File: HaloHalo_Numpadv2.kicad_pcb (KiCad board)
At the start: 2 copper layers, 108.7 x 105.4 mm, 92 parts, among them SW1 SW_SPST, SW10 SW_SPST, SW11 SW_SPST, SW12 SW_SPST, SW13 SW_SPST, SW14 SW_SPST, SW15 SW_SPST, SW16 SW_SPST, SW17 SW_SPST, SW18 SW_SPST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

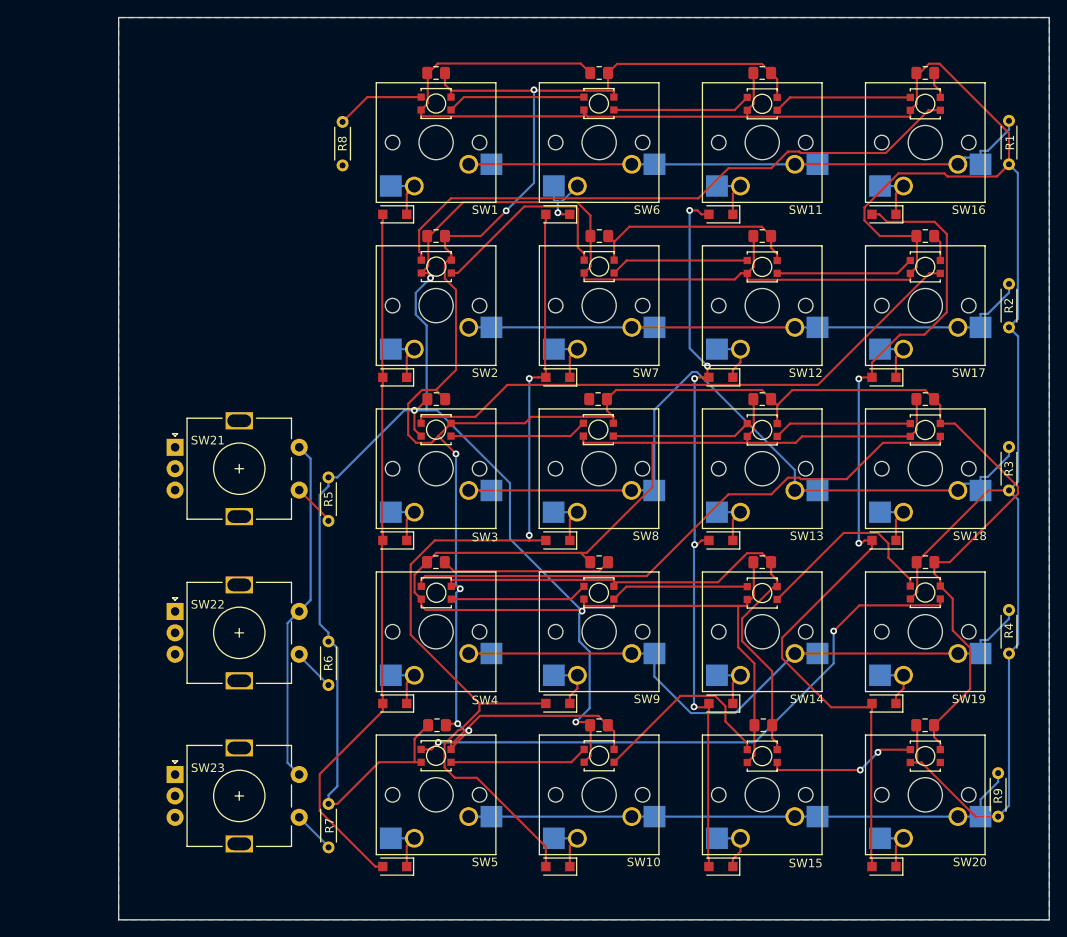
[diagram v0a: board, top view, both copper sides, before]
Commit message: Updated Schematic and PCB to include headers for OLED display. Need to update corresponding PDFs and images.
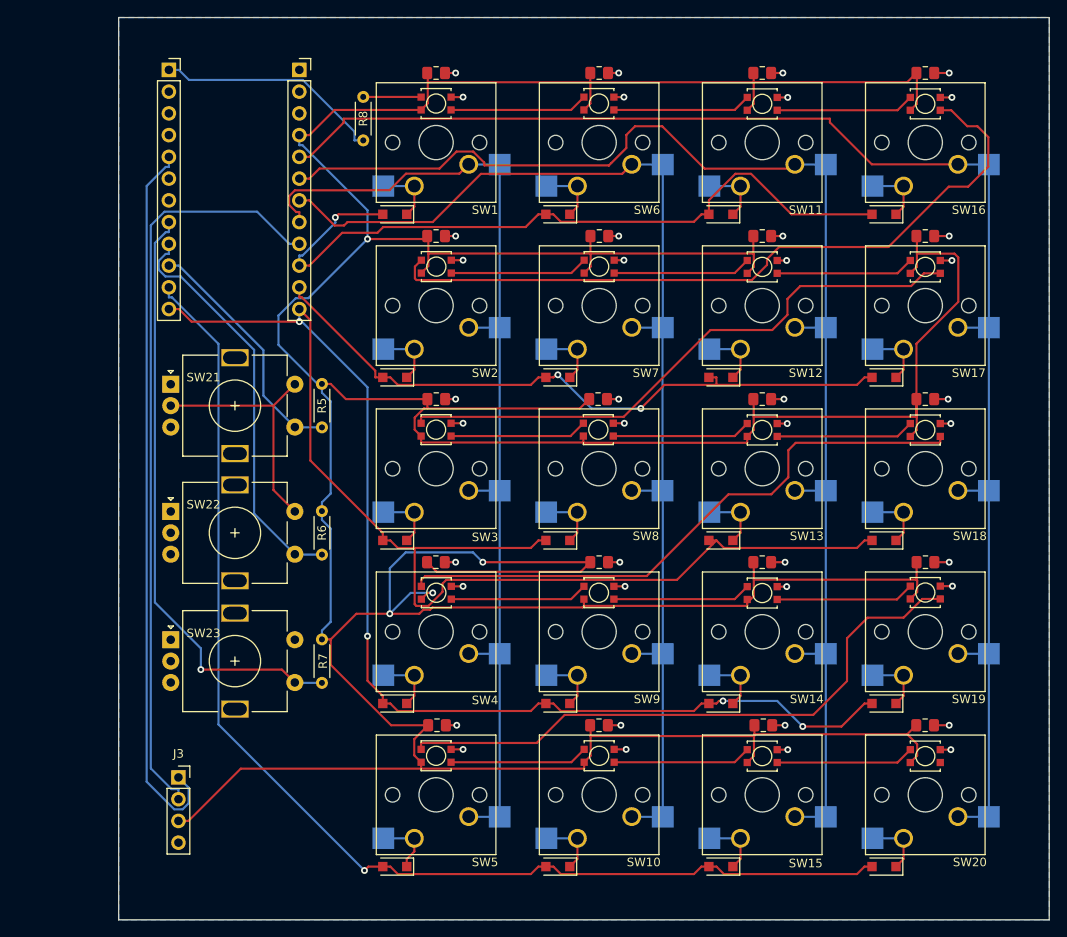
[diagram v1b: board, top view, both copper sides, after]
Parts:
- removed R1, R2, R3, R4, R9: 4.7k, Resistor_THT:R_Axial_DIN0204_L3.6mm_D1.6mm_P5.08mm_Horizontal
- added J1: Conn_01x12_Female, Connector_PinSocket_2.54mm:PinSocket_1x12_P2.54mm_Vertical, F.Cu at (91.8, 51.3)
- added J2: Conn_01x12_Female, Connector_PinSocket_2.54mm:PinSocket_1x12_P2.54mm_Vertical, F.Cu at (107.1, 51.3)
- added J3: Conn_01x04_Female, Connector_PinSocket_2.54mm:PinSocket_1x04_P2.54mm_Vertical, F.Cu at (93.0, 134.0)
- moved R7 19.2 mm to (109.7, 122.9)
- moved SW23 15.8 mm to (92.1, 117.9)
- moved R6 15.3 mm to (109.7, 108.0)
- moved SW22 11.7 mm to (92.1, 102.9)
- moved R5 10.9 mm to (109.7, 93.1)
- moved SW21 7.38 mm to (92.1, 88.1)
- moved R8 3.79 mm to (114.6, 54.5)
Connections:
- C1 pad 2: GNDD -> GND
- C10 pad 2: GNDD -> GND
- C11 pad 2: GNDD -> GND
- C12 pad 2: GNDD -> GND
- C13 pad 2: GNDD -> GND
- C14 pad 2: GNDD -> GND
- C15 pad 2: GNDD -> GND
- C16 pad 2: GNDD -> GND
- C17 pad 2: GNDD -> GND
- C18 pad 2: GNDD -> GND
- C19 pad 2: GNDD -> GND
- C2 pad 2: GNDD -> GND
- C20 pad 2: GNDD -> GND
- C3 pad 2: GNDD -> GND
- C4 pad 2: GNDD -> GND
- C5 pad 2: GNDD -> GND
- C6 pad 2: GNDD -> GND
- C7 pad 2: GNDD -> GND
- C8 pad 2: GNDD -> GND
- C9 pad 2: GNDD -> GND
- D1 pad 3: GNDD -> GND
- D10 pad 3: GNDD -> GND
- D11 pad 3: GNDD -> GND
- D12 pad 3: GNDD -> GND
- D13 pad 3: GNDD -> GND
- D14 pad 3: GNDD -> GND
- D15 pad 3: GNDD -> GND
- D16 pad 3: GNDD -> GND
- D17 pad 3: GNDD -> GND
- D18 pad 3: GNDD -> GND
- D19 pad 3: GNDD -> GND
- D2 pad 3: GNDD -> GND
- D20 pad 3: GNDD -> GND
- D21 pad 2: C1 -> R1
- D22 pad 2: C1 -> R2
- D23 pad 2: C1 -> R3
- D24 pad 2: C1 -> R4
- D25 pad 2: C1 -> R5
- D26 pad 2: C2 -> R1
- D27 pad 2: C2 -> R2
- D28 pad 2: C2 -> R3
- D29 pad 2: C2 -> R4
- D3 pad 3: GNDD -> GND
- D30 pad 2: C2 -> R5
- D31 pad 2: C3 -> R1
- D32 pad 2: C3 -> R2
- D33 pad 2: C3 -> R3
- D34 pad 2: C3 -> R4
- D35 pad 2: C3 -> R5
- D36 pad 2: C4 -> R1
- D37 pad 2: C4 -> R2
- D38 pad 2: C4 -> R3
- D39 pad 2: C4 -> R4
- D4 pad 3: GNDD -> GND
- D40 pad 2: C4 -> R5
- D5 pad 3: GNDD -> GND
- D6 pad 3: GNDD -> GND
- D7 pad 3: GNDD -> GND
- D8 pad 3: GNDD -> GND
- D9 pad 3: GNDD -> GND
- SW1 pad 2: R1 -> C1
- SW10 pad 2: R5 -> C2
- SW11 pad 2: R1 -> C3
- SW12 pad 2: R2 -> C3
- SW13 pad 2: R3 -> C3
- SW14 pad 2: R4 -> C3
- SW15 pad 2: R5 -> C3
- SW16 pad 2: R1 -> C4
- SW17 pad 2: R2 -> C4
- SW18 pad 2: R3 -> C4
- SW19 pad 2: R4 -> C4
- SW2 pad 2: R2 -> C1
- SW20 pad 2: R5 -> C4
- SW21 pad S2: RotSW_C1 -> GND
- SW22 pad S2: RotSW_C1 -> GND
- SW23 pad S2: RotSW_C1 -> GND
- SW3 pad 2: R3 -> C1
- SW4 pad 2: R4 -> C1
- SW5 pad 2: R5 -> C1
- SW6 pad 2: R1 -> C2
- SW7 pad 2: R2 -> C2
- SW8 pad 2: R3 -> C2
- SW9 pad 2: R4 -> C2
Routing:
- net GNDD: track 412.6 -> 0.00 mm, vias 6 -> 0
- net SCL: track 0.00 -> 88.4 mm
- net SDA: track 0.00 -> 84.3 mm
- net GND: track 0.00 -> 83.7 mm, vias 0 -> 40
- net C3: track 85.7 -> 159.5 mm, vias 5 -> 0
- net R5: track 65.7 -> 139.5 mm, vias 0 -> 1
- net C4: track 104.3 -> 175.9 mm, vias 2 -> 0
- net RotSW_R3: track 4.93 -> 70.2 mm, vias 0 -> 1
- net R4: track 79.4 -> 127.3 mm, vias 0 -> 4
- net RotSW_R2: track 5.01 -> 47.8 mm
- net RotSW_C1: track 40.5 -> 0.00 mm
- net C1: track 83.4 -> 120.6 mm
- net LED_DIN: track 0.00 -> 26.7 mm
- net C2: track 111.6 -> 137.4 mm, vias 2 -> 0
- net R3: track 90.7 -> 116.3 mm
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
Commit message: Added OLED display headers
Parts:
- removed R5, R6, R7: 4.7k, Resistor_THT:R_Axial_DIN0204_L3.6mm_D1.6mm_P5.08mm_Horizontal
- added HOLE5: MountingHole_4mm, Keyboard-Parts:MountingHole_M2, F.Cu at (109.1, 126.4)
- added HOLE5: MountingHole_4mm, Keyboard-Parts:MountingHole_M2, F.Cu at (103.4, 74.3)
- added HOLE5: MountingHole_4mm, Keyboard-Parts:MountingHole_M2, F.Cu at (190.4, 49.5)
- added HOLE5: MountingHole_4mm, Keyboard-Parts:MountingHole_M2, F.Cu at (78.5, 49.5)
- added HOLE5: MountingHole_4mm, Keyboard-Parts:MountingHole_M2, F.Cu at (152.0, 78.0)
- added HOLE5: MountingHole_4mm, Keyboard-Parts:MountingHole_M2, F.Cu at (190.4, 146.3)
- added HOLE5: MountingHole_4mm, Keyboard-Parts:MountingHole_M2, F.Cu at (152.0, 116.1)
- added HOLE5: MountingHole_4mm, Keyboard-Parts:MountingHole_M2, F.Cu at (78.5, 146.3)
- moved J3 41.5 mm to (88.6, 92.7), turned to -90 degrees
- moved SW23 16.0 mm to (95.5, 133.5)
- moved SW22 12.1 mm to (95.5, 114.5)
- moved SW21 8.13 mm to (95.5, 95.4)
- moved J1 3.48 mm to (95.2, 52.1)
- moved J2 3.48 mm to (110.5, 52.1)
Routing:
- net SCL: track 88.4 -> 34.2 mm
- net SDA: track 84.3 -> 33.2 mm
- net GND: track 83.7 -> 54.8 mm
- net VCC: track 624.8 -> 643.3 mm, vias 4 -> 3
- net R1: track 88.3 -> 74.5 mm, vias 1 -> 0
- net RotSW_R1: track 28.8 -> 38.5 mm, vias 0 -> 1
- net C1: track 120.6 -> 113.8 mm
- net RotSW_R3: track 70.2 -> 76.4 mm
- net RotSW_R2: track 47.8 -> 53.4 mm, vias 0 -> 1
- net C2: track 137.4 -> 131.9 mm, vias 0 -> 1
- net C4: track 175.9 -> 172.5 mm
- net LED_DIN: track 26.7 -> 23.5 mm
- net C3: track 159.5 -> 156.4 mm
- net R4: track 127.3 -> 124.5 mm, vias 4 -> 3
- net R5: track 139.5 -> 137.3 mm
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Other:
- board size 108.7 x 105.4 mm -> 120.5 x 105.4 mm

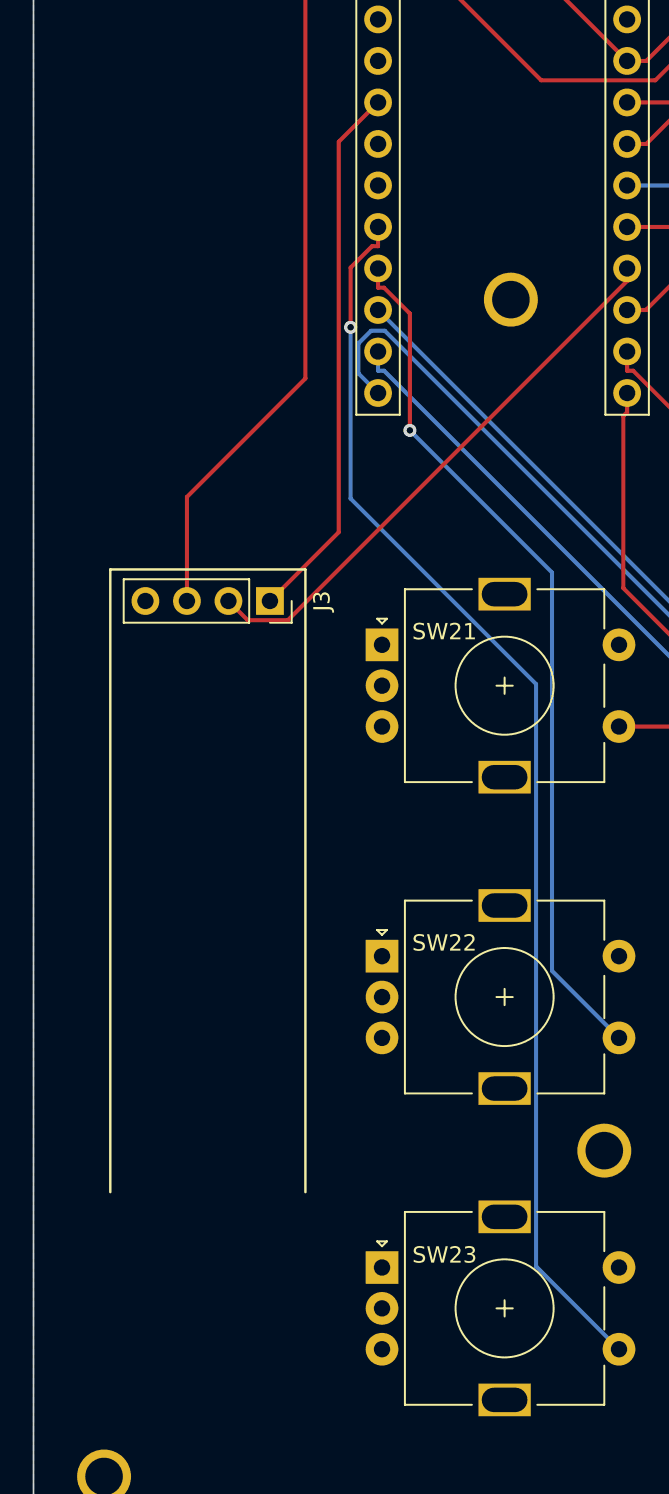
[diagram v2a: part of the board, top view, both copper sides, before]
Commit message: Added silkscreen images to PCB
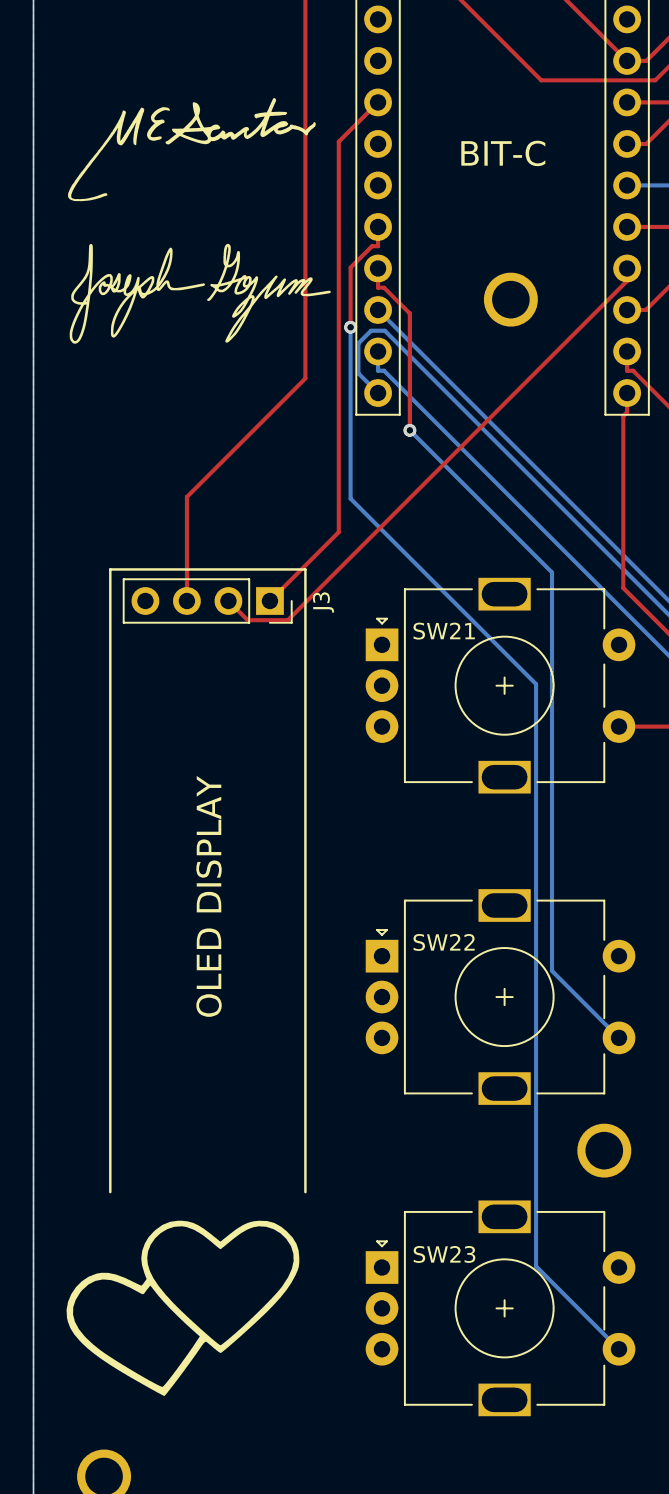
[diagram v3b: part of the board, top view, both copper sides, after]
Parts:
- added G1: LOGO, LOGO, F.Cu at (84.1, 65.3)
- added G2: LOGO, LOGO, F.Cu at (84.5, 74.0)
- added G3: LOGO, LOGO, F.Cu at (84.7, 119.3)
- added Hearts: LOGO, LOGO, F.Cu at (83.3, 135.8)
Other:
- board text added: "BIT-C"
- board text added: "Halo-Halo Numpad Designed by Joseph Gozum Version 1.0"
- board text added: "OLED DISPLAY"
